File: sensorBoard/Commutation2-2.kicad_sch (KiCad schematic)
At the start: 14 parts, among them Q10 2N7002, U20 BTS50080-1TEA

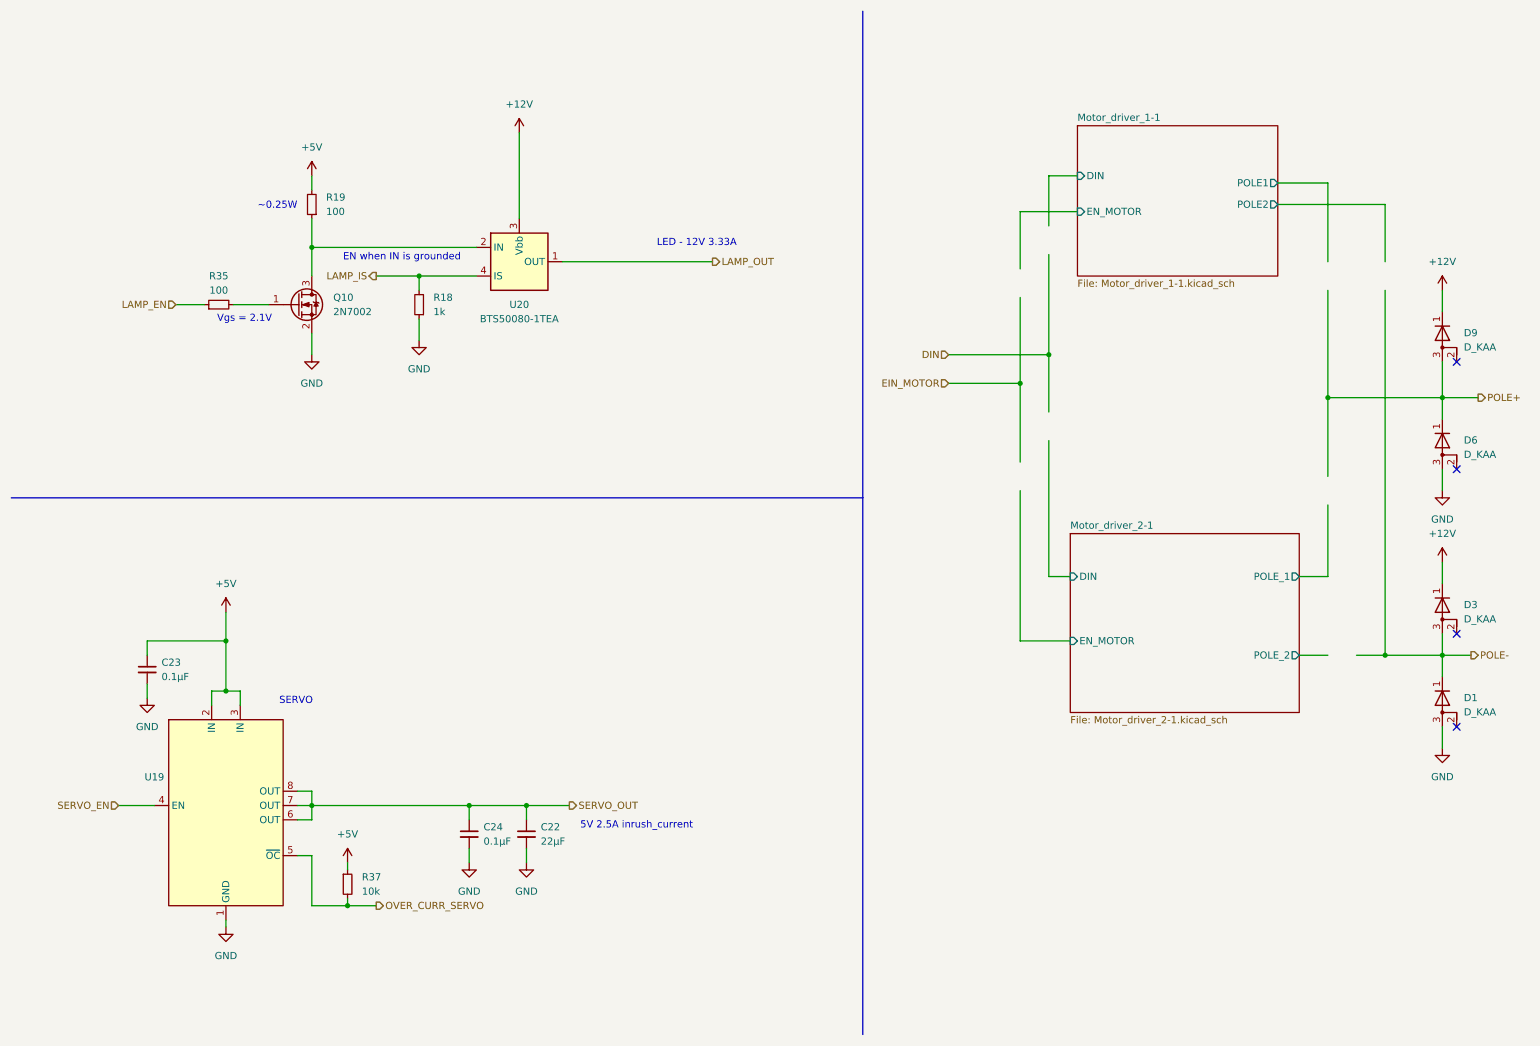
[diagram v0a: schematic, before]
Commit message: new two separate pcbs
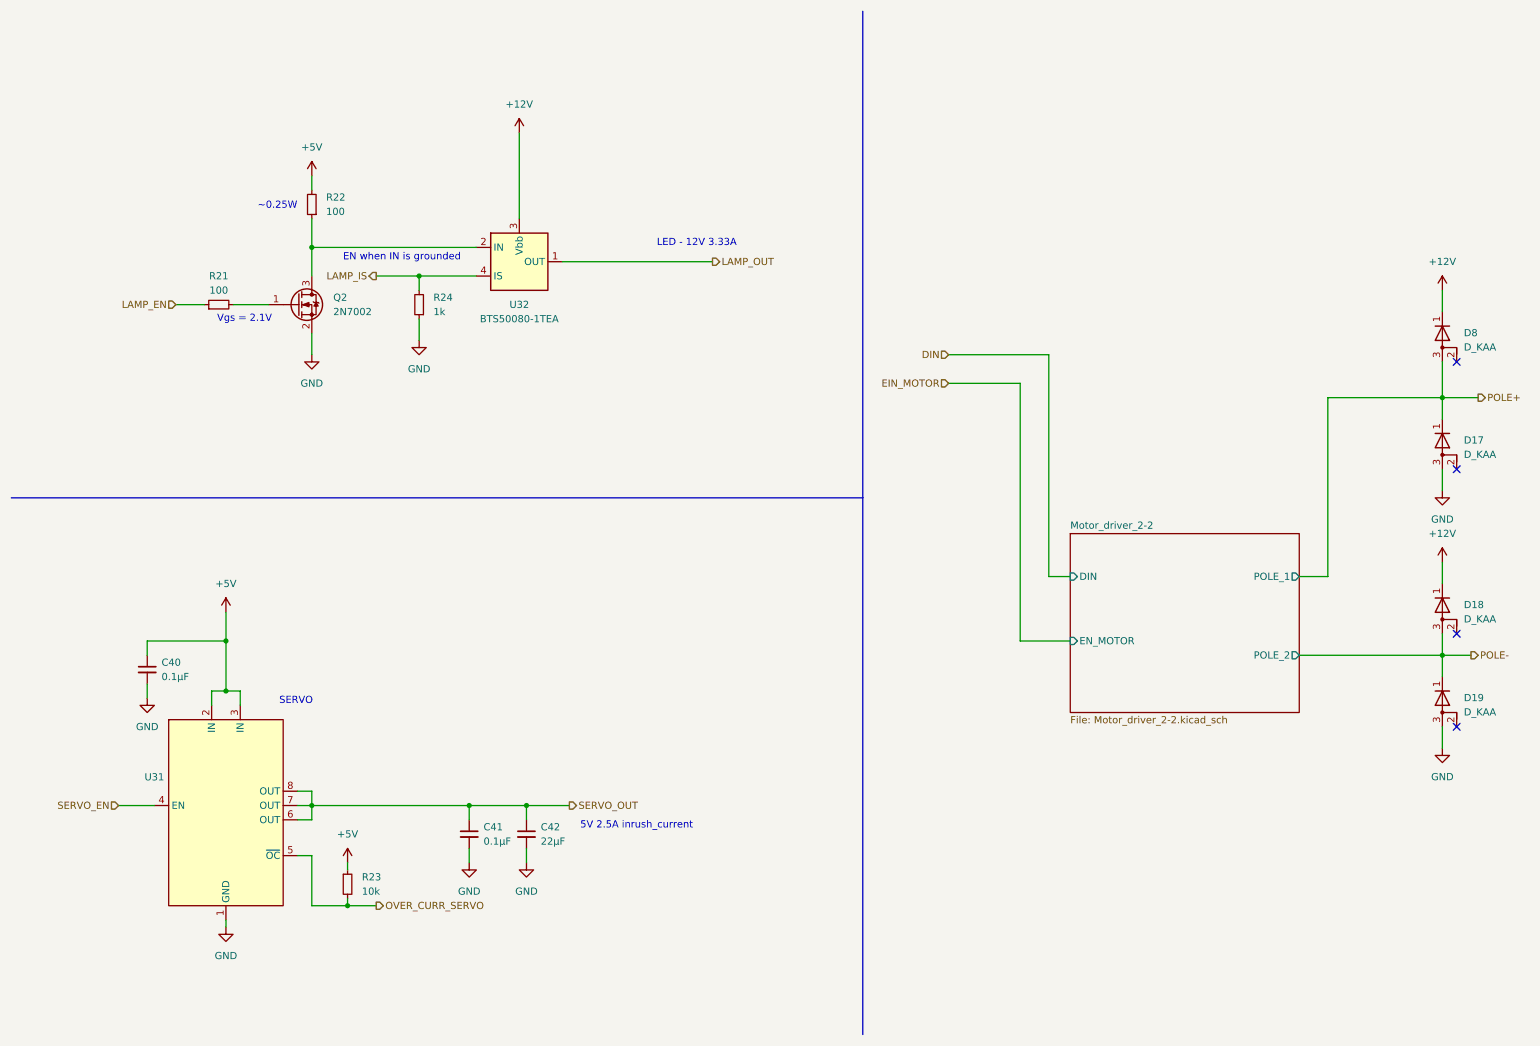
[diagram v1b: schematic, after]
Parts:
- renumbered C23 to C40, C24 to C41, C22 to C42, D6 to D17, D3 to D18, D1 to D19, D9 to D8, Q10 to Q2, R35 to R21, R19 to R22, R37 to R23, R18 to R24, U19 to U31, U20 to U32
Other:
- sheet Motor_driver_2-1 renamed Motor_driver_2-2
- removed sheet Motor_driver_1-1
- sheet Motor_driver_2-2: file Motor_driver_2-1.kicad_sch -> Motor_driver_2-2.kicad_sch
